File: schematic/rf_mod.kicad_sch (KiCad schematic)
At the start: 0 parts

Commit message: completed sound block, finished cart io port, and finished decoder.
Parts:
- added L15: 42uH, symbol Device:L
- added R18: 1K8, symbol Device:R
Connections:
- new net SND_CLK: L15.2
- new net SND_OUT: R18.2
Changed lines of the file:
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@@
 (kicad_sch (version 20211123) (generator eeschema)
   (paper "A4")
+  (hierarchical_label "SND_OUT" (shape input) (at 151.13 135.89 0)
+    (effects (font (size 1.27 1.27)) (justify left))
+  )
+  (hierarchical_label "SND_CLK" (shape input) (at 151.13 146.05 0)
+    (effects (font (size 1.27 1.27)) (justify left))
+  )
+  (symbol (lib_id "Device:L") (at 147.32 146.05 90) (unit 1)
+    (in_bom yes) (on_board yes) (fields_autoplaced)
+    (property "Reference" "L15" (id 0) (at 147.32 139.7 90))
+    (property "Value" "42uH" (id 1) (at 147.32 142.24 90))
+    (property "Footprint" "" (id 2) (at 147.32 146.05 0)
+      (effects (font (size 1.27 1.27)) hide)
+    )
+    (property "Datasheet" "~" (id 3) (at 147.32 146.05 0)
+      (effects (font (size 1.27 1.27)) hide)
+    )
+    (pin "1")
+    (pin "2")
+  )
+  (symbol (lib_id "Device:R") (at 147.32 135.89 90) (unit 1)
+    (in_bom yes) (on_board yes) (fields_autoplaced)
+    (property "Reference" "R18" (id 0) (at 147.32 129.54 90))
+    (property "Value" "1K8" (id 1) (at 147.32 132.08 90))
+    (property "Footprint" "" (id 2) (at 147.32 137.668 90)
+      (effects (font (size 1.27 1.27)) hide)
+    )
+    (property "Datasheet" "~" (id 3) (at 147.32 135.89 0)
+      (effects (font (size 1.27 1.27)) hide)
+    )
+    (pin "1")
+    (pin "2")
+  )
 )

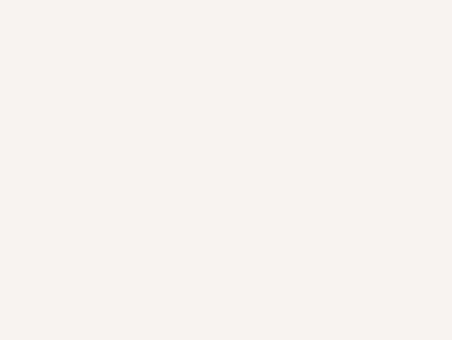
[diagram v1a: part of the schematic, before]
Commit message: fixed some more line names, added a expansion port io pin.
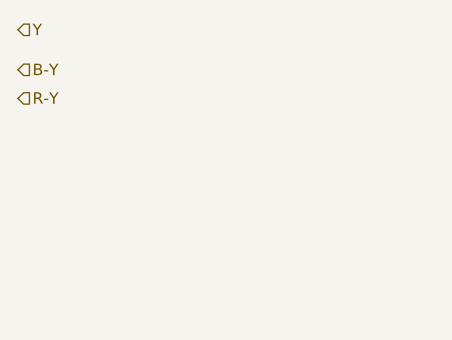
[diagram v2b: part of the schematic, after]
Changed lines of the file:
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@@
 (kicad_sch (version 20211123) (generator eeschema)
   (paper "A4")
+  (hierarchical_label "R-Y" (shape input) (at 83.185 122.555 0)
+    (effects (font (size 1.27 1.27)) (justify left))
+  )
   (hierarchical_label "SND_OUT" (shape input) (at 151.13 135.89 0)
     (effects (font (size 1.27 1.27)) (justify left))
@@
     (effects (font (size 1.27 1.27)) (justify left))
   )
+  (hierarchical_label "Y" (shape input) (at 83.185 114.935 0)
+    (effects (font (size 1.27 1.27)) (justify left))
+  )
+  (hierarchical_label "B-Y" (shape input) (at 83.185 119.38 0)
+    (effects (font (size 1.27 1.27)) (justify left))
+  )

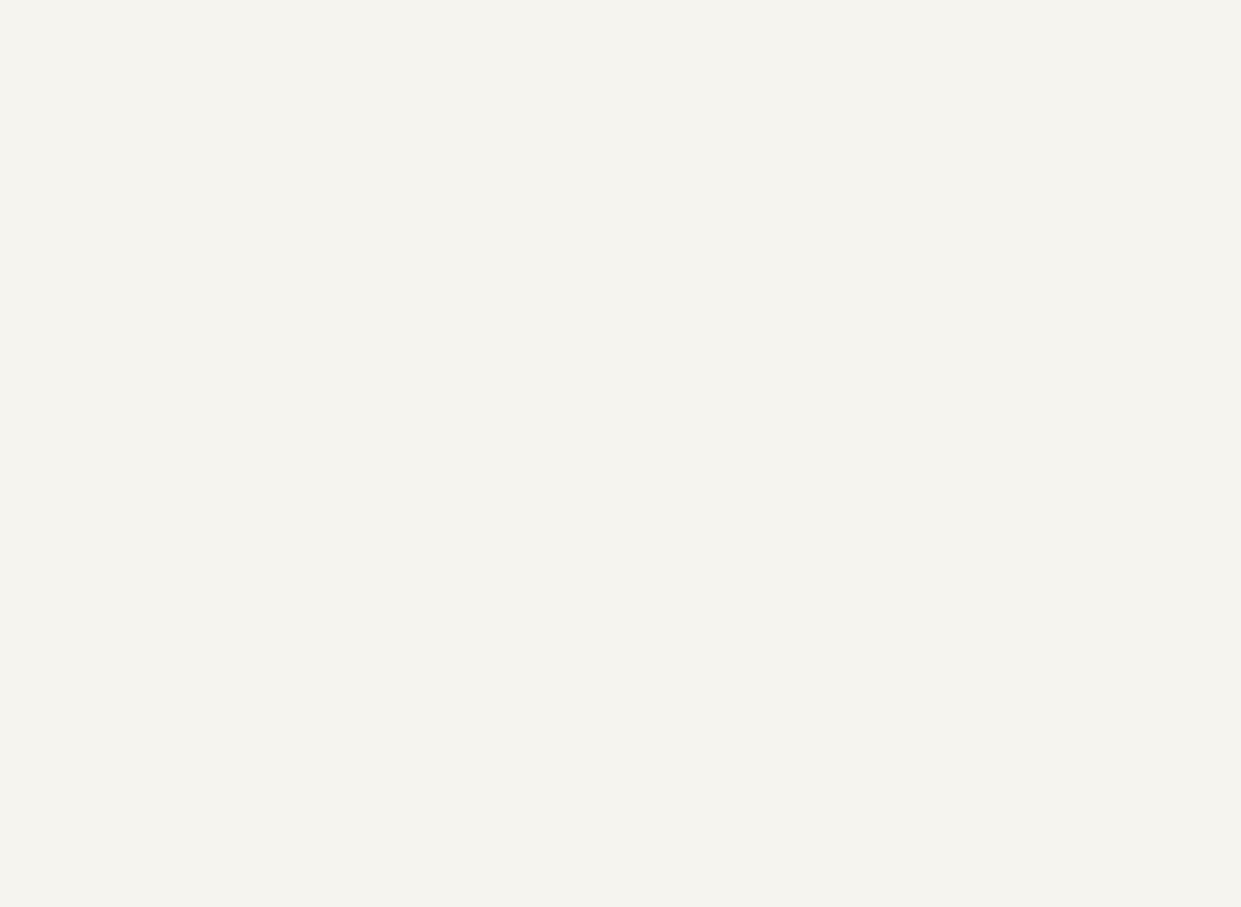
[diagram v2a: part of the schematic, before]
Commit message: power supply added, controller circuit added. Controller is a very odd duck to say the least. Seems they wanted to have plenty of current, maybe due to the steering wheel attachement?
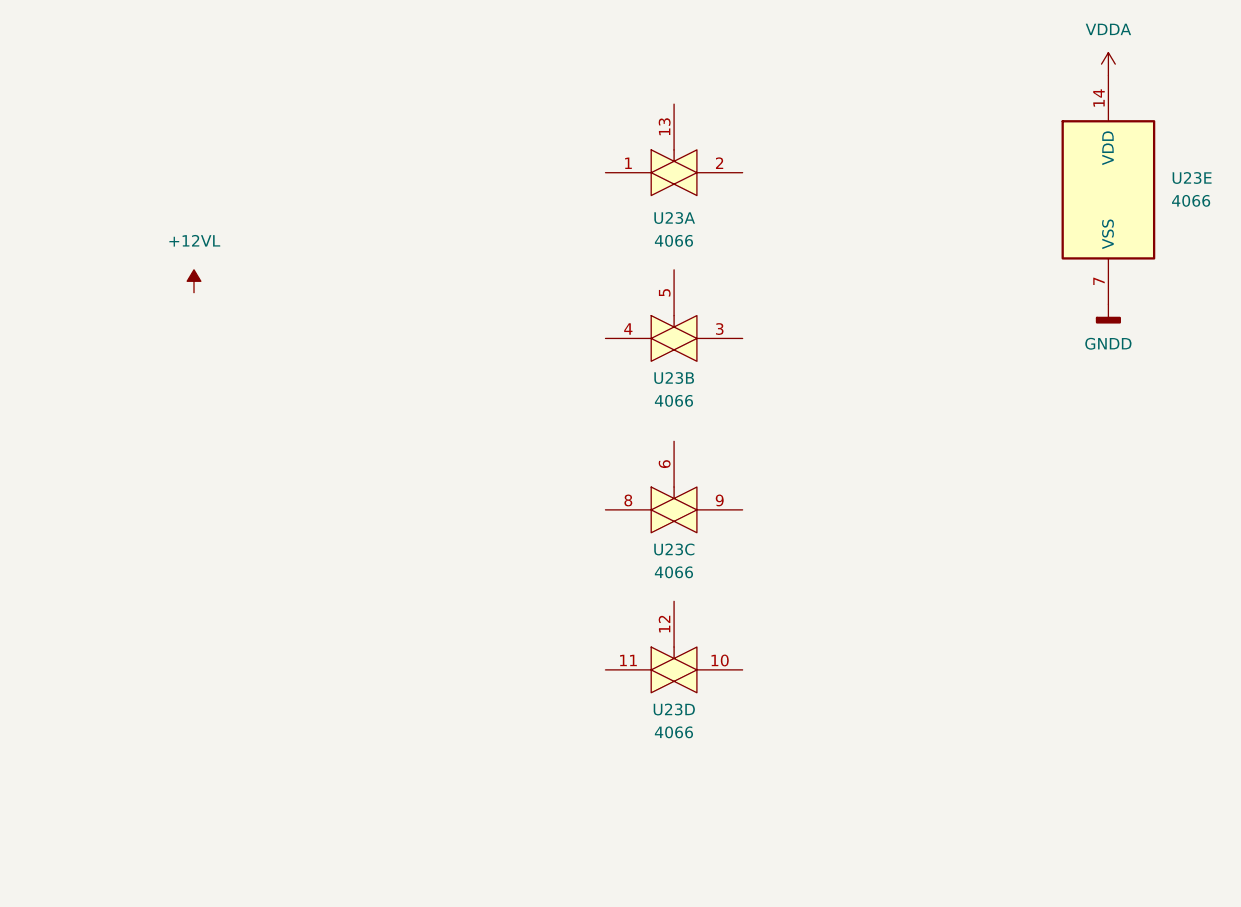
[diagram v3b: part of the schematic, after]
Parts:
- added U23: 4066, symbol 4xxx:4066
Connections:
- new net GNDD: U23.7 (VSS)
- new net VDDA: U23.14 (VDD)
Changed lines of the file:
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@@
     (pin "2")
+  )
+  (symbol (lib_id "4xxx:4066") (at 217.805 48.895 0) (unit 5)
+    (in_bom yes) (on_board yes) (fields_autoplaced)
+    (property "Reference" "U23" (id 0) (at 224.79 47.6249 0)
+      (effects (font (size 1.27 1.27)) (justify left))
+    )
+    (property "Value" "4066" (id 1) (at 224.79 50.1649 0)
+      (effects (font (size 1.27 1.27)) (justify left))
+    )
+    (property "Footprint" "" (id 2) (at 217.805 48.895 0)
+      (effects (font (size 1.27 1.27)) hide)
+    )
+    (property "Datasheet" "http://www.ti.com/lit/ds/symlink/cd4066b.pdf" (id 3) (at 217.805 48.895 0)
+      (effects (font (size 1.27 1.27)) hide)
+    )
+    (pin "1")
+    (pin "13")
+    (pin "2")
+    (pin "3")
+    (pin "4")
+    (pin "5")
+    (pin "6")
+    (pin "8")
+    (pin "9")
+    (pin "10")
+    (pin "11")
+    (pin "12")
+    (pin "14")
+    (pin "7")
+  )
+  (symbol (lib_id "4xxx:4066") (at 169.545 84.455 0) (unit 3)
+    (in_bom yes) (on_board yes) (fields_autoplaced)
+    (property "Reference" "U23" (id 0) (at 169.545 88.9 0))
+    (property "Value" "4066" (id 1) (at 169.545 91.44 0))
+    (property "Footprint" "" (id 2) (at 169.545 84.455 0)
+      (effects (font (size 1.27 1.27)) hide)
+    )
+    (property "Datasheet" "http://www.ti.com/lit/ds/symlink/cd4066b.pdf" (id 3) (at 169.545 84.455 0)
+      (effects (font (size 1.27 1.27)) hide)
+    )
+    (pin "1")
+    (pin "13")
+    (pin "2")
+    (pin "3")
+    (pin "4")
+    (pin "5")
+    (pin "6")
+    (pin "8")
+    (pin "9")
+    (pin "10")
+    (pin "11")
+    (pin "12")
+    (pin "14")
+    (pin "7")
+  )
+  (symbol (lib_id "4xxx:4066") (at 169.545 46.99 0) (unit 1)
+    (in_bom yes) (on_board yes) (fields_autoplaced)
+    (property "Reference" "U23" (id 0) (at 169.545 52.07 0))
+    (property "Value" "4066" (id 1) (at 169.545 54.61 0))
+    (property "Footprint" "" (id 2) (at 169.545 46.99 0)
+      (effects (font (size 1.27 1.27)) hide)
+    )
+    (property "Datasheet" "http://www.ti.com/lit/ds/symlink/cd4066b.pdf" (id 3) (at 169.545 46.99 0)
+      (effects (font (size 1.27 1.27)) hide)
+    )
+    (pin "1")
+    (pin "13")
+    (pin "2")
+    (pin "3")
+    (pin "4")
+    (pin "5")
+    (pin "6")
+    (pin "8")
+    (pin "9")
+    (pin "10")
+    (pin "11")
+    (pin "12")
+    (pin "14")
+    (pin "7")
+  )
+  (symbol (lib_id "power:VDDA") (at 217.805 36.195 0) (unit 1)
+    (in_bom yes) (on_board yes) (fields_autoplaced)
+    (property "Reference" "#PWR?" (id 0) (at 217.805 40.005 0)
+      (effects (font (size 1.27 1.27)) hide)
+    )
+    (property "Value" "VDDA" (id 1) (at 217.805 31.115 0))
+    (property "Footprint" "" (id 2) (at 217.805 36.195 0)
+      (effects (font (size 1.27 1.27)) hide)
+    )
+    (property "Datasheet" "" (id 3) (at 217.805 36.195 0)
+      (effects (font (size 1.27 1.27)) hide)
+    )
+    (pin "1")
+  )
+  (symbol (lib_id "4xxx:4066") (at 169.545 65.405 0) (unit 2)
+    (in_bom yes) (on_board yes) (fields_autoplaced)
+    (property "Reference" "U23" (id 0) (at 169.545 69.85 0))
+    (property "Value" "4066" (id 1) (at 169.545 72.39 0))
+    (property "Footprint" "" (id 2) (at 169.545 65.405 0)
+      (effects (font (size 1.27 1.27)) hide)
+    )
+    (property "Datasheet" "http://www.ti.com/lit/ds/symlink/cd4066b.pdf" (id 3) (at 169.545 65.405 0)
+      (effects (font (size 1.27 1.27)) hide)
+    )
+    (pin "1")
+    (pin "13")
+    (pin "2")
+    (pin "3")
+    (pin "4")
+    (pin "5")
+    (pin "6")
+    (pin "8")
+    (pin "9")
+    (pin "10")
+    (pin "11")
+    (pin "12")
+    (pin "14")
+    (pin "7")
   )
   (symbol (lib_id "Device:R") (at 147.32 135.89 90) (unit 1)
@@
     (pin "2")
   )
+  (symbol (lib_id "power:GNDD") (at 217.805 61.595 0) (unit 1)
+    (in_bom yes) (on_board yes) (fields_autoplaced)
+    (property "Reference" "#PWR?" (id 0) (at 217.805 67.945 0)
+      (effects (font (size 1.27 1.27)) hide)
+    )
+    (property "Value" "GNDD" (id 1) (at 217.805 66.04 0))
+    (property "Footprint" "" (id 2) (at 217.805 61.595 0)
+      (effects (font (size 1.27 1.27)) hide)
+    )
+    (property "Datasheet" "" (id 3) (at 217.805 61.595 0)
+      (effects (font (size 1.27 1.27)) hide)
+    )
+    (pin "1")
+  )
+  (symbol (lib_id "4xxx:4066") (at 169.545 102.235 0) (unit 4)
+    (in_bom yes) (on_board yes) (fields_autoplaced)
+    (property "Reference" "U23" (id 0) (at 169.545 106.68 0))
+    (property "Value" "4066" (id 1) (at 169.545 109.22 0))
+    (property "Footprint" "" (id 2) (at 169.545 102.235 0)
+      (effects (font (size 1.27 1.27)) hide)
+    )
+    (property "Datasheet" "http://www.ti.com/lit/ds/symlink/cd4066b.pdf" (id 3) (at 169.545 102.235 0)
+      (effects (font (size 1.27 1.27)) hide)
+    )
+    (pin "1")
+    (pin "13")
+    (pin "2")
+    (pin "3")
+    (pin "4")
+    (pin "5")
+    (pin "6")
+    (pin "8")
+    (pin "9")
+    (pin "10")
+    (pin "11")
+    (pin "12")
+    (pin "14")
+    (pin "7")
+  )
+  (symbol (lib_id "Power_Symbols:+12VL") (at 116.205 60.325 0) (unit 1)
+    (in_bom yes) (on_board yes) (fields_autoplaced)
+    (property "Reference" "#PWR?" (id 0) (at 116.205 57.785 0)
+      (effects (font (size 1.27 1.27)) hide)
+    )
+    (property "Value" "+12VL" (id 1) (at 116.205 54.61 0))
+    (property "Footprint" "" (id 2) (at 116.205 60.325 0)
+      (effects (font (size 1.27 1.27)) hide)
+    )
+    (property "Datasheet" "" (id 3) (at 116.205 60.325 0)
+      (effects (font (size 1.27 1.27)) hide)
+    )
+    (pin "1")
+  )
 )

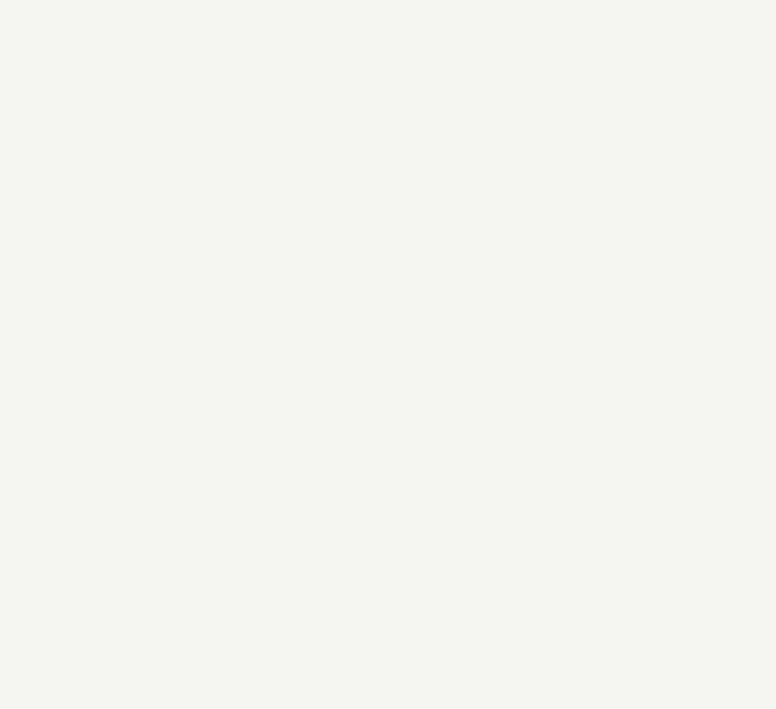
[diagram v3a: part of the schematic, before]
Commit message: started work on clock_reset_misc circuits. inverter u7 done, u8 added and starting work around U22.
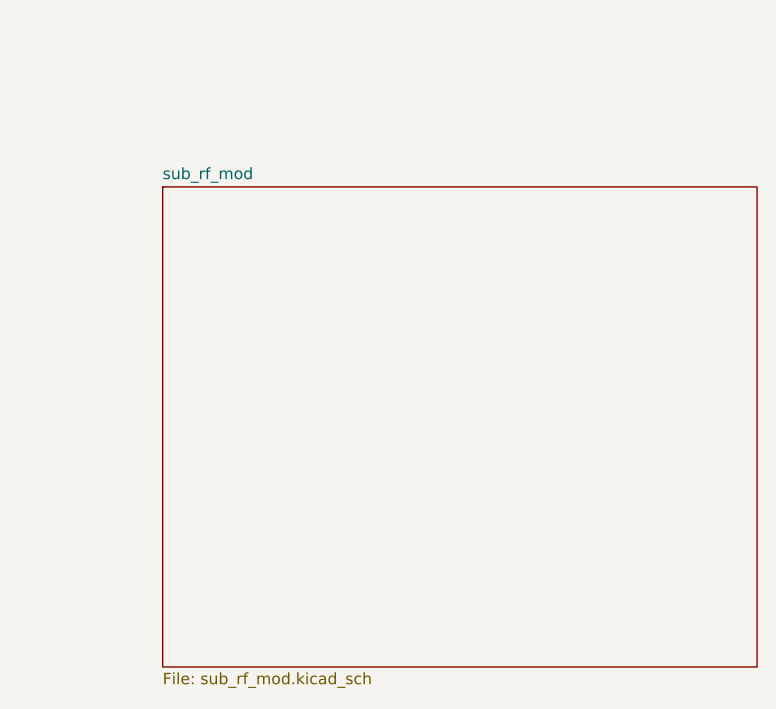
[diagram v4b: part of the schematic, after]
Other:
- added sheet sub_rf_mod (sub_rf_mod.kicad_sch)
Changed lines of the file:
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@@
     (pin "1")
   )
+  (sheet (at 195.58 94.615) (size 66.04 53.34) (fields_autoplaced)
+    (stroke (width 0.1524) (type solid) (color 0 0 0 0))
+    (fill (color 0 0 0 0.0000))
+    (property "Sheet name" "sub_rf_mod" (id 0) (at 195.58 93.9034 0)
+      (effects (font (size 1.27 1.27)) (justify left bottom))
+    )
+    (property "Sheet file" "sub_rf_mod.kicad_sch" (id 1) (at 195.58 148.5396 0)
+      (effects (font (size 1.27 1.27)) (justify left top))
+    )
+  )
 )

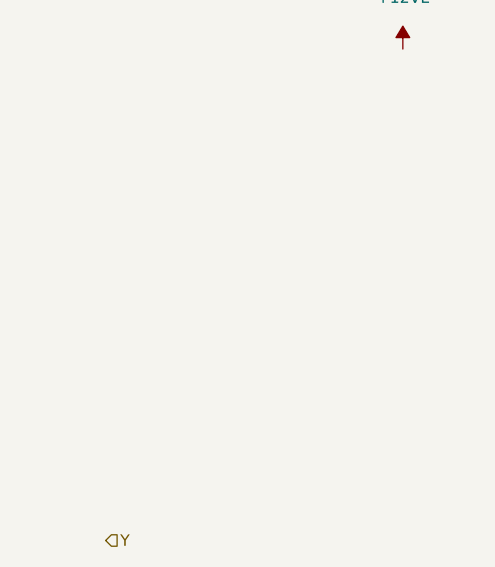
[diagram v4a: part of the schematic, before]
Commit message: altered and did some cleanup of the way the wires were run. Finished expansion port routes to rf modulator. Added ext_psu for future external power supply design (will be an off the shelf psu block).
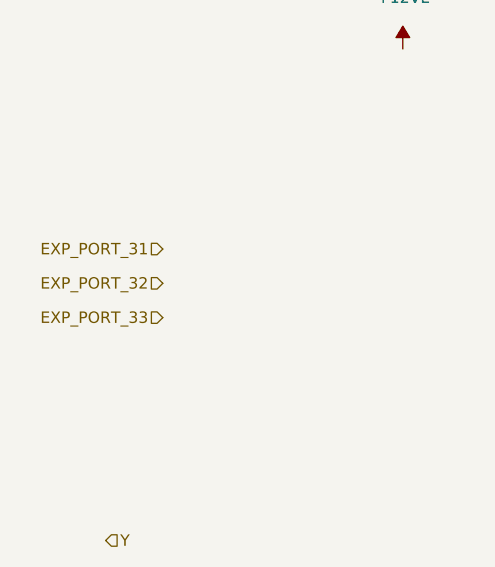
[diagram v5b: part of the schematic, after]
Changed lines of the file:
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@@
     (effects (font (size 1.27 1.27)) (justify left))
+  )
+  (hierarchical_label "EXP_PORT_31" (shape input) (at 89.535 82.55 180)
+    (effects (font (size 1.27 1.27)) (justify right))
   )
   (hierarchical_label "SND_OUT" (shape input) (at 151.13 135.89 0)
@@
     (effects (font (size 1.27 1.27)) (justify left))
   )
+  (hierarchical_label "EXP_PORT_33" (shape input) (at 89.535 90.17 180)
+    (effects (font (size 1.27 1.27)) (justify right))
+  )
   (hierarchical_label "B-Y" (shape input) (at 83.185 119.38 0)
     (effects (font (size 1.27 1.27)) (justify left))
   )
+  (hierarchical_label "EXP_PORT_32" (shape input) (at 89.535 86.36 180)
+    (effects (font (size 1.27 1.27)) (justify right))
+  )
   (symbol (lib_id "Device:L") (at 147.32 146.05 90) (unit 1)
